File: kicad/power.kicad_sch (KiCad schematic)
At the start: 15 parts, among them U2 MAX16956

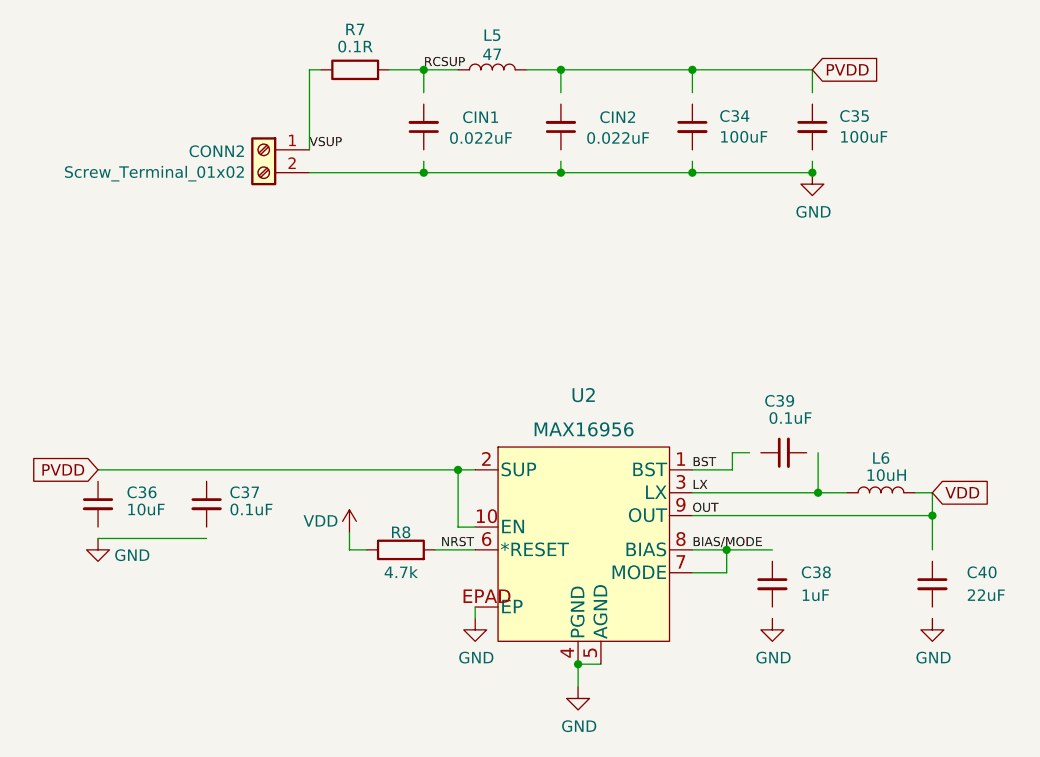
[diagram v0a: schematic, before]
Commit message: generated pdf schematic
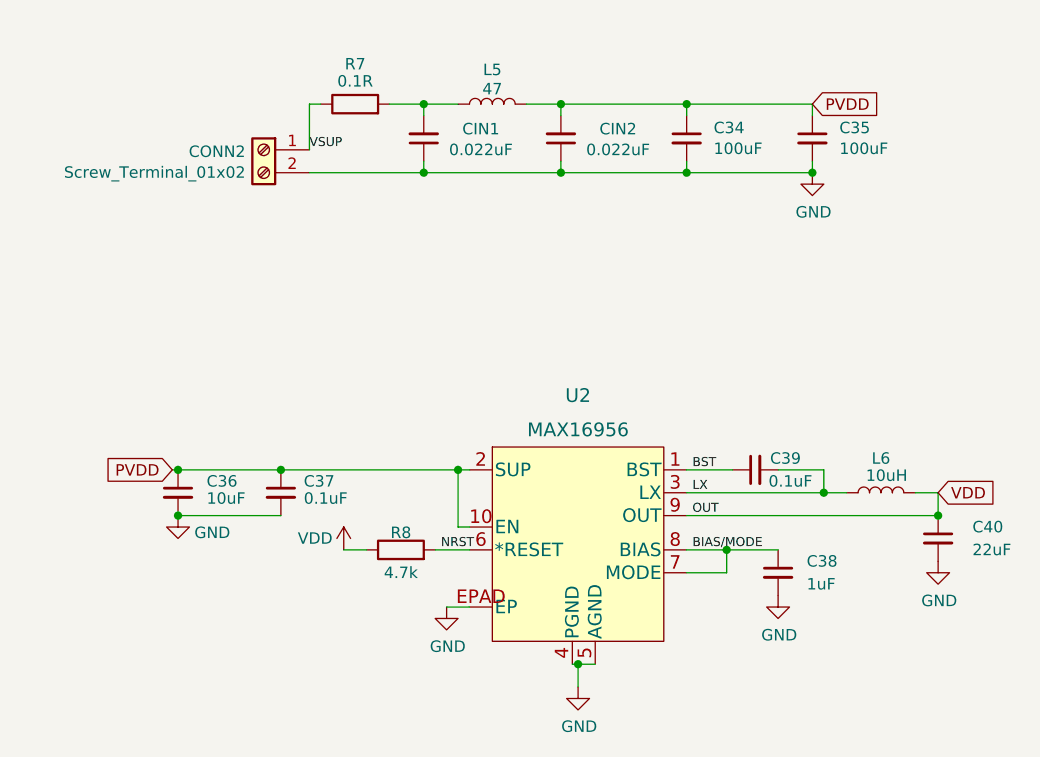
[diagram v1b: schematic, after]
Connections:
- net RCSUP is gone; now on an unnamed net: L5.1, R7.2
- net BIAS/MODE: now also C38.1
- net BST: now also C39.1
- net GND: now also C34.2, C35.2, C36.2, C37.2, C38.2, C40.2, CIN1.1, CIN2.1
- net LX: now also C39.2
- net PVDD: now also C34.1, C35.1, C36.1, C37.1, CIN2.2
- net VDD: now also C40.1
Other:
- moved on the sheet: C34, C35, C36, C37, C38, C39, C40, CIN1, CIN2, L5, R7, U2
